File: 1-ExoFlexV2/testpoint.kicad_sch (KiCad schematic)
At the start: 154 parts

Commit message: Schématisation terminée
- Schéma terminé
- Passage vers le PCB
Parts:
- TP1: renamed from TP?; value R1DAMP1 -> TestPoint; DESCRIPTION Compact THM Test Point -Red -> PC TEST POINT COMPACT RED; MANUFACTURER (none) -> Keystone Electronics; PACKAGE NON STANDARD-1 Keystone -> 0.125" Dia x 0.220" L; PART NUMBER (none) -> 5005; TYPE (none) -> Through Hole
- TP10: renamed from TP?; value LLC1 -> TestPoint; DESCRIPTION Compact THM Test Point -Red -> PC TEST POINT COMPACT RED; MANUFACTURER (none) -> Keystone Electronics; PACKAGE NON STANDARD-1 Keystone -> 0.125" Dia x 0.220" L; PART NUMBER (none) -> 5005; TYPE (none) -> Through Hole
- TP100: renamed from TP?; value SSWMAX -> TestPoint; DESCRIPTION Compact THM Test Point -Red -> PC TEST POINT COMPACT RED; MANUFACTURER (none) -> Keystone Electronics; PACKAGE NON STANDARD-1 Keystone -> 0.125" Dia x 0.220" L; PART NUMBER (none) -> 5005; TYPE (none) -> Through Hole
- TP101, TP111, TP112, TP113, TP119, TP120, TP129, TP136, TP137, TP139, TP146, TP148: renamed from TP?; value GND -> TestPoint; DESCRIPTION Compact THM Test Point -Red -> PC TEST POINT COMPACT RED; MANUFACTURER (none) -> Keystone Electronics; PACKAGE NON STANDARD-1 Keystone -> 0.125" Dia x 0.220" L; PART NUMBER (none) -> 5005; TYPE (none) -> Through Hole
- TP102: renamed from TP?; value URG_SEC -> TestPoint; DESCRIPTION Compact THM Test Point -Red -> PC TEST POINT COMPACT RED; MANUFACTURER (none) -> Keystone Electronics; PACKAGE NON STANDARD-1 Keystone -> 0.125" Dia x 0.220" L; PART NUMBER (none) -> 5005; TYPE (none) -> Through Hole
- TP103: renamed from TP?; value SR&L -> TestPoint; DESCRIPTION Compact THM Test Point -Red -> PC TEST POINT COMPACT RED; MANUFACTURER (none) -> Keystone Electronics; PACKAGE NON STANDARD-1 Keystone -> 0.125" Dia x 0.220" L; PART NUMBER (none) -> 5005; TYPE (none) -> Through Hole
- TP104: renamed from TP?; value SINT1 -> TestPoint; DESCRIPTION Compact THM Test Point -Red -> PC TEST POINT COMPACT RED; MANUFACTURER (none) -> Keystone Electronics; PACKAGE NON STANDARD-1 Keystone -> 0.125" Dia x 0.220" L; PART NUMBER (none) -> 5005; TYPE (none) -> Through Hole
- TP105: renamed from TP?; value R1FSR1 -> TestPoint; DESCRIPTION Compact THM Test Point -Red -> PC TEST POINT COMPACT RED; MANUFACTURER (none) -> Keystone Electronics; PACKAGE NON STANDARD-1 Keystone -> 0.125" Dia x 0.220" L; PART NUMBER (none) -> 5005; TYPE (none) -> Through Hole
- TP106: renamed from TP?; value R2FSR1 -> TestPoint; DESCRIPTION Compact THM Test Point -Red -> PC TEST POINT COMPACT RED; MANUFACTURER (none) -> Keystone Electronics; PACKAGE NON STANDARD-1 Keystone -> 0.125" Dia x 0.220" L; PART NUMBER (none) -> 5005; TYPE (none) -> Through Hole
- TP107: renamed from TP?; value R1FSR2 -> TestPoint; DESCRIPTION Compact THM Test Point -Red -> PC TEST POINT COMPACT RED; MANUFACTURER (none) -> Keystone Electronics; PACKAGE NON STANDARD-1 Keystone -> 0.125" Dia x 0.220" L; PART NUMBER (none) -> 5005; TYPE (none) -> Through Hole
- TP108: renamed from TP?; value R2FSR2 -> TestPoint; DESCRIPTION Compact THM Test Point -Red -> PC TEST POINT COMPACT RED; MANUFACTURER (none) -> Keystone Electronics; PACKAGE NON STANDARD-1 Keystone -> 0.125" Dia x 0.220" L; PART NUMBER (none) -> 5005; TYPE (none) -> Through Hole
- TP109: renamed from TP?; value R1FSR3 -> TestPoint; DESCRIPTION Compact THM Test Point -Red -> PC TEST POINT COMPACT RED; MANUFACTURER (none) -> Keystone Electronics; PACKAGE NON STANDARD-1 Keystone -> 0.125" Dia x 0.220" L; PART NUMBER (none) -> 5005; TYPE (none) -> Through Hole
- TP11: renamed from TP?; value CLC1 -> TestPoint; DESCRIPTION Compact THM Test Point -Red -> PC TEST POINT COMPACT RED; MANUFACTURER (none) -> Keystone Electronics; PACKAGE NON STANDARD-1 Keystone -> 0.125" Dia x 0.220" L; PART NUMBER (none) -> 5005; TYPE (none) -> Through Hole
- TP110: renamed from TP?; value R2FSR3 -> TestPoint; DESCRIPTION Compact THM Test Point -Red -> PC TEST POINT COMPACT RED; MANUFACTURER (none) -> Keystone Electronics; PACKAGE NON STANDARD-1 Keystone -> 0.125" Dia x 0.220" L; PART NUMBER (none) -> 5005; TYPE (none) -> Through Hole
- TP114: renamed from TP?; value SINT2 -> TestPoint; DESCRIPTION Compact THM Test Point -Red -> PC TEST POINT COMPACT RED; MANUFACTURER (none) -> Keystone Electronics; PACKAGE NON STANDARD-1 Keystone -> 0.125" Dia x 0.220" L; PART NUMBER (none) -> 5005; TYPE (none) -> Through Hole
- TP115: renamed from TP?; value R1DANA1 -> TestPoint; DESCRIPTION Compact THM Test Point -Red -> PC TEST POINT COMPACT RED; MANUFACTURER (none) -> Keystone Electronics; PACKAGE NON STANDARD-1 Keystone -> 0.125" Dia x 0.220" L; PART NUMBER (none) -> 5005; TYPE (none) -> Through Hole
- TP116: renamed from TP?; value R2DANA1 -> TestPoint; DESCRIPTION Compact THM Test Point -Red -> PC TEST POINT COMPACT RED; MANUFACTURER (none) -> Keystone Electronics; PACKAGE NON STANDARD-1 Keystone -> 0.125" Dia x 0.220" L; PART NUMBER (none) -> 5005; TYPE (none) -> Through Hole
- TP117: renamed from TP?; value R1DANA2 -> TestPoint; DESCRIPTION Compact THM Test Point -Red -> PC TEST POINT COMPACT RED; MANUFACTURER (none) -> Keystone Electronics; PACKAGE NON STANDARD-1 Keystone -> 0.125" Dia x 0.220" L; PART NUMBER (none) -> 5005; TYPE (none) -> Through Hole
- TP118: renamed from TP?; value R2DANA2 -> TestPoint; DESCRIPTION Compact THM Test Point -Red -> PC TEST POINT COMPACT RED; MANUFACTURER (none) -> Keystone Electronics; PACKAGE NON STANDARD-1 Keystone -> 0.125" Dia x 0.220" L; PART NUMBER (none) -> 5005; TYPE (none) -> Through Hole
- TP12: renamed from TP?; value R1DAMP2 -> TestPoint; DESCRIPTION Compact THM Test Point -Red -> PC TEST POINT COMPACT RED; MANUFACTURER (none) -> Keystone Electronics; PACKAGE NON STANDARD-1 Keystone -> 0.125" Dia x 0.220" L; PART NUMBER (none) -> 5005; TYPE (none) -> Through Hole
- TP121: renamed from TP?; value SINT3 -> TestPoint; DESCRIPTION Compact THM Test Point -Red -> PC TEST POINT COMPACT RED; MANUFACTURER (none) -> Keystone Electronics; PACKAGE NON STANDARD-1 Keystone -> 0.125" Dia x 0.220" L; PART NUMBER (none) -> 5005; TYPE (none) -> Through Hole
- TP122: renamed from TP?; value 24V -> TestPoint; DESCRIPTION Compact THM Test Point -Red -> PC TEST POINT COMPACT RED; MANUFACTURER (none) -> Keystone Electronics; PACKAGE NON STANDARD-1 Keystone -> 0.125" Dia x 0.220" L; PART NUMBER (none) -> 5005; TYPE (none) -> Through Hole
- TP123: renamed from TP?; value 5VNUM -> TestPoint; DESCRIPTION Compact THM Test Point -Red -> PC TEST POINT COMPACT RED; MANUFACTURER (none) -> Keystone Electronics; PACKAGE NON STANDARD-1 Keystone -> 0.125" Dia x 0.220" L; PART NUMBER (none) -> 5005; TYPE (none) -> Through Hole
- TP124: renamed from TP?; value R1EM2 -> TestPoint; DESCRIPTION Compact THM Test Point -Red -> PC TEST POINT COMPACT RED; MANUFACTURER (none) -> Keystone Electronics; PACKAGE NON STANDARD-1 Keystone -> 0.125" Dia x 0.220" L; PART NUMBER (none) -> 5005; TYPE (none) -> Through Hole
- TP125: renamed from TP?; value R2EM2 -> TestPoint; DESCRIPTION Compact THM Test Point -Red -> PC TEST POINT COMPACT RED; MANUFACTURER (none) -> Keystone Electronics; PACKAGE NON STANDARD-1 Keystone -> 0.125" Dia x 0.220" L; PART NUMBER (none) -> 5005; TYPE (none) -> Through Hole
- TP126: renamed from TP?; value BUTPROXL1 -> TestPoint; DESCRIPTION Compact THM Test Point -Red -> PC TEST POINT COMPACT RED; MANUFACTURER (none) -> Keystone Electronics; PACKAGE NON STANDARD-1 Keystone -> 0.125" Dia x 0.220" L; PART NUMBER (none) -> 5005; TYPE (none) -> Through Hole
- TP127: renamed from TP?; value BUTPROXR2 -> TestPoint; DESCRIPTION Compact THM Test Point -Red -> PC TEST POINT COMPACT RED; MANUFACTURER (none) -> Keystone Electronics; PACKAGE NON STANDARD-1 Keystone -> 0.125" Dia x 0.220" L; PART NUMBER (none) -> 5005; TYPE (none) -> Through Hole
- TP128: renamed from TP?; value DSW&INT -> TestPoint; DESCRIPTION Compact THM Test Point -Red -> PC TEST POINT COMPACT RED; MANUFACTURER (none) -> Keystone Electronics; PACKAGE NON STANDARD-1 Keystone -> 0.125" Dia x 0.220" L; PART NUMBER (none) -> 5005; TYPE (none) -> Through Hole
- TP13: renamed from TP?; value R2DAMP2 -> TestPoint; DESCRIPTION Compact THM Test Point -Red -> PC TEST POINT COMPACT RED; MANUFACTURER (none) -> Keystone Electronics; PACKAGE NON STANDARD-1 Keystone -> 0.125" Dia x 0.220" L; PART NUMBER (none) -> 5005; TYPE (none) -> Through Hole
- TP130: renamed from TP?; value RELAY -> TestPoint; DESCRIPTION Compact THM Test Point -Red -> PC TEST POINT COMPACT RED; MANUFACTURER (none) -> Keystone Electronics; PACKAGE NON STANDARD-1 Keystone -> 0.125" Dia x 0.220" L; PART NUMBER (none) -> 5005; TYPE (none) -> Through Hole
- TP131: renamed from TP?; value RESET -> TestPoint; DESCRIPTION Compact THM Test Point -Red -> PC TEST POINT COMPACT RED; MANUFACTURER (none) -> Keystone Electronics; PACKAGE NON STANDARD-1 Keystone -> 0.125" Dia x 0.220" L; PART NUMBER (none) -> 5005; TYPE (none) -> Through Hole
- TP132: renamed from TP?; value R1RE2 -> TestPoint; DESCRIPTION Compact THM Test Point -Red -> PC TEST POINT COMPACT RED; MANUFACTURER (none) -> Keystone Electronics; PACKAGE NON STANDARD-1 Keystone -> 0.125" Dia x 0.220" L; PART NUMBER (none) -> 5005; TYPE (none) -> Through Hole
- TP133: renamed from TP?; value R2RE2 -> TestPoint; DESCRIPTION Compact THM Test Point -Red -> PC TEST POINT COMPACT RED; MANUFACTURER (none) -> Keystone Electronics; PACKAGE NON STANDARD-1 Keystone -> 0.125" Dia x 0.220" L; PART NUMBER (none) -> 5005; TYPE (none) -> Through Hole
- TP134: renamed from TP?; value BUTPROXL2 -> TestPoint; DESCRIPTION Compact THM Test Point -Red -> PC TEST POINT COMPACT RED; MANUFACTURER (none) -> Keystone Electronics; PACKAGE NON STANDARD-1 Keystone -> 0.125" Dia x 0.220" L; PART NUMBER (none) -> 5005; TYPE (none) -> Through Hole
- TP135: renamed from TP?; value OPTO1 -> TestPoint; DESCRIPTION Compact THM Test Point -Red -> PC TEST POINT COMPACT RED; MANUFACTURER (none) -> Keystone Electronics; PACKAGE NON STANDARD-1 Keystone -> 0.125" Dia x 0.220" L; PART NUMBER (none) -> 5005; TYPE (none) -> Through Hole
- TP138: renamed from TP?; value CAN_RD -> TestPoint; DESCRIPTION Compact THM Test Point -Red -> PC TEST POINT COMPACT RED; MANUFACTURER (none) -> Keystone Electronics; PACKAGE NON STANDARD-1 Keystone -> 0.125" Dia x 0.220" L; PART NUMBER (none) -> 5005; TYPE (none) -> Through Hole
- TP14: renamed from TP?; value R1DLAMP2 -> TestPoint; DESCRIPTION Compact THM Test Point -Red -> PC TEST POINT COMPACT RED; MANUFACTURER (none) -> Keystone Electronics; PACKAGE NON STANDARD-1 Keystone -> 0.125" Dia x 0.220" L; PART NUMBER (none) -> 5005; TYPE (none) -> Through Hole
- TP140: renamed from TP?; value 5VA -> TestPoint; DESCRIPTION Compact THM Test Point -Red -> PC TEST POINT COMPACT RED; MANUFACTURER (none) -> Keystone Electronics; PACKAGE NON STANDARD-1 Keystone -> 0.125" Dia x 0.220" L; PART NUMBER (none) -> 5005; TYPE (none) -> Through Hole
- TP141: renamed from TP?; value 5VA- -> TestPoint; DESCRIPTION Compact THM Test Point -Red -> PC TEST POINT COMPACT RED; MANUFACTURER (none) -> Keystone Electronics; PACKAGE NON STANDARD-1 Keystone -> 0.125" Dia x 0.220" L; PART NUMBER (none) -> 5005; TYPE (none) -> Through Hole
- TP142: renamed from TP?; value R1EM1 -> TestPoint; DESCRIPTION Compact THM Test Point -Red -> PC TEST POINT COMPACT RED; MANUFACTURER (none) -> Keystone Electronics; PACKAGE NON STANDARD-1 Keystone -> 0.125" Dia x 0.220" L; PART NUMBER (none) -> 5005; TYPE (none) -> Through Hole
- TP143: renamed from TP?; value R2EM1 -> TestPoint; DESCRIPTION Compact THM Test Point -Red -> PC TEST POINT COMPACT RED; MANUFACTURER (none) -> Keystone Electronics; PACKAGE NON STANDARD-1 Keystone -> 0.125" Dia x 0.220" L; PART NUMBER (none) -> 5005; TYPE (none) -> Through Hole
- TP144: renamed from TP?; value BUTPROXR1 -> TestPoint; DESCRIPTION Compact THM Test Point -Red -> PC TEST POINT COMPACT RED; MANUFACTURER (none) -> Keystone Electronics; PACKAGE NON STANDARD-1 Keystone -> 0.125" Dia x 0.220" L; PART NUMBER (none) -> 5005; TYPE (none) -> Through Hole
- TP145: renamed from TP?; value OPTO2 -> TestPoint; DESCRIPTION Compact THM Test Point -Red -> PC TEST POINT COMPACT RED; MANUFACTURER (none) -> Keystone Electronics; PACKAGE NON STANDARD-1 Keystone -> 0.125" Dia x 0.220" L; PART NUMBER (none) -> 5005; TYPE (none) -> Through Hole
- TP147: renamed from TP?; value CAN_TD -> TestPoint; DESCRIPTION Compact THM Test Point -Red -> PC TEST POINT COMPACT RED; MANUFACTURER (none) -> Keystone Electronics; PACKAGE NON STANDARD-1 Keystone -> 0.125" Dia x 0.220" L; PART NUMBER (none) -> 5005; TYPE (none) -> Through Hole
- TP149: renamed from TP?; value LATCH -> TestPoint; DESCRIPTION Compact THM Test Point -Red -> PC TEST POINT COMPACT RED; MANUFACTURER (none) -> Keystone Electronics; PACKAGE NON STANDARD-1 Keystone -> 0.125" Dia x 0.220" L; PART NUMBER (none) -> 5005; TYPE (none) -> Through Hole
- TP15: renamed from TP?; value R2DLAMP2 -> TestPoint; DESCRIPTION Compact THM Test Point -Red -> PC TEST POINT COMPACT RED; MANUFACTURER (none) -> Keystone Electronics; PACKAGE NON STANDARD-1 Keystone -> 0.125" Dia x 0.220" L; PART NUMBER (none) -> 5005; TYPE (none) -> Through Hole
- TP150, TP33: renamed from TP?; value SALIM -> TestPoint; DESCRIPTION Compact THM Test Point -Red -> PC TEST POINT COMPACT RED; MANUFACTURER (none) -> Keystone Electronics; PACKAGE NON STANDARD-1 Keystone -> 0.125" Dia x 0.220" L; PART NUMBER (none) -> 5005; TYPE (none) -> Through Hole
- TP151: renamed from TP?; value R1RE1 -> TestPoint; DESCRIPTION Compact THM Test Point -Red -> PC TEST POINT COMPACT RED; MANUFACTURER (none) -> Keystone Electronics; PACKAGE NON STANDARD-1 Keystone -> 0.125" Dia x 0.220" L; PART NUMBER (none) -> 5005; TYPE (none) -> Through Hole
- TP152: renamed from TP?; value R2RE1 -> TestPoint; DESCRIPTION Compact THM Test Point -Red -> PC TEST POINT COMPACT RED; MANUFACTURER (none) -> Keystone Electronics; PACKAGE NON STANDARD-1 Keystone -> 0.125" Dia x 0.220" L; PART NUMBER (none) -> 5005; TYPE (none) -> Through Hole
- TP153: renamed from TP?; value SOPTO -> TestPoint; DESCRIPTION Compact THM Test Point -Red -> PC TEST POINT COMPACT RED; MANUFACTURER (none) -> Keystone Electronics; PACKAGE NON STANDARD-1 Keystone -> 0.125" Dia x 0.220" L; PART NUMBER (none) -> 5005; TYPE (none) -> Through Hole
- TP154: renamed from TP?; value SBUTPROX -> TestPoint; DESCRIPTION Compact THM Test Point -Red -> PC TEST POINT COMPACT RED; MANUFACTURER (none) -> Keystone Electronics; PACKAGE NON STANDARD-1 Keystone -> 0.125" Dia x 0.220" L; PART NUMBER (none) -> 5005; TYPE (none) -> Through Hole
- TP16: renamed from TP?; value SGAMP2 -> TestPoint; DESCRIPTION Compact THM Test Point -Red -> PC TEST POINT COMPACT RED; MANUFACTURER (none) -> Keystone Electronics; PACKAGE NON STANDARD-1 Keystone -> 0.125" Dia x 0.220" L; PART NUMBER (none) -> 5005; TYPE (none) -> Through Hole
- TP17: renamed from TP?; value LAMP2 -> TestPoint; DESCRIPTION Compact THM Test Point -Red -> PC TEST POINT COMPACT RED; MANUFACTURER (none) -> Keystone Electronics; PACKAGE NON STANDARD-1 Keystone -> 0.125" Dia x 0.220" L; PART NUMBER (none) -> 5005; TYPE (none) -> Through Hole
- TP18: renamed from TP?; value CAMP2 -> TestPoint; DESCRIPTION Compact THM Test Point -Red -> PC TEST POINT COMPACT RED; MANUFACTURER (none) -> Keystone Electronics; PACKAGE NON STANDARD-1 Keystone -> 0.125" Dia x 0.220" L; PART NUMBER (none) -> 5005; TYPE (none) -> Through Hole
- TP19: renamed from TP?; value SGLC2 -> TestPoint; DESCRIPTION Compact THM Test Point -Red -> PC TEST POINT COMPACT RED; MANUFACTURER (none) -> Keystone Electronics; PACKAGE NON STANDARD-1 Keystone -> 0.125" Dia x 0.220" L; PART NUMBER (none) -> 5005; TYPE (none) -> Through Hole
- TP2: renamed from TP?; value R2DAMP1 -> TestPoint; DESCRIPTION Compact THM Test Point -Red -> PC TEST POINT COMPACT RED; MANUFACTURER (none) -> Keystone Electronics; PACKAGE NON STANDARD-1 Keystone -> 0.125" Dia x 0.220" L; PART NUMBER (none) -> 5005; TYPE (none) -> Through Hole
- TP20: renamed from TP?; value LLC2 -> TestPoint; DESCRIPTION Compact THM Test Point -Red -> PC TEST POINT COMPACT RED; MANUFACTURER (none) -> Keystone Electronics; PACKAGE NON STANDARD-1 Keystone -> 0.125" Dia x 0.220" L; PART NUMBER (none) -> 5005; TYPE (none) -> Through Hole
- TP21: renamed from TP?; value CLC2 -> TestPoint; DESCRIPTION Compact THM Test Point -Red -> PC TEST POINT COMPACT RED; MANUFACTURER (none) -> Keystone Electronics; PACKAGE NON STANDARD-1 Keystone -> 0.125" Dia x 0.220" L; PART NUMBER (none) -> 5005; TYPE (none) -> Through Hole
- TP22: renamed from TP?; value SGLC3 -> TestPoint; DESCRIPTION Compact THM Test Point -Red -> PC TEST POINT COMPACT RED; MANUFACTURER (none) -> Keystone Electronics; PACKAGE NON STANDARD-1 Keystone -> 0.125" Dia x 0.220" L; PART NUMBER (none) -> 5005; TYPE (none) -> Through Hole
- TP23: renamed from TP?; value LLC3 -> TestPoint; DESCRIPTION Compact THM Test Point -Red -> PC TEST POINT COMPACT RED; MANUFACTURER (none) -> Keystone Electronics; PACKAGE NON STANDARD-1 Keystone -> 0.125" Dia x 0.220" L; PART NUMBER (none) -> 5005; TYPE (none) -> Through Hole
- TP24: renamed from TP?; value CLC3 -> TestPoint; DESCRIPTION Compact THM Test Point -Red -> PC TEST POINT COMPACT RED; MANUFACTURER (none) -> Keystone Electronics; PACKAGE NON STANDARD-1 Keystone -> 0.125" Dia x 0.220" L; PART NUMBER (none) -> 5005; TYPE (none) -> Through Hole
- TP25: renamed from TP?; value SLCPOS -> TestPoint; DESCRIPTION Compact THM Test Point -Red -> PC TEST POINT COMPACT RED; MANUFACTURER (none) -> Keystone Electronics; PACKAGE NON STANDARD-1 Keystone -> 0.125" Dia x 0.220" L; PART NUMBER (none) -> 5005; TYPE (none) -> Through Hole
- TP26: renamed from TP?; value R1DAMP3 -> TestPoint; DESCRIPTION Compact THM Test Point -Red -> PC TEST POINT COMPACT RED; MANUFACTURER (none) -> Keystone Electronics; PACKAGE NON STANDARD-1 Keystone -> 0.125" Dia x 0.220" L; PART NUMBER (none) -> 5005; TYPE (none) -> Through Hole
- TP27: renamed from TP?; value R2DAMP3 -> TestPoint; DESCRIPTION Compact THM Test Point -Red -> PC TEST POINT COMPACT RED; MANUFACTURER (none) -> Keystone Electronics; PACKAGE NON STANDARD-1 Keystone -> 0.125" Dia x 0.220" L; PART NUMBER (none) -> 5005; TYPE (none) -> Through Hole
- TP28: renamed from TP?; value R1DLAMP3 -> TestPoint; DESCRIPTION Compact THM Test Point -Red -> PC TEST POINT COMPACT RED; MANUFACTURER (none) -> Keystone Electronics; PACKAGE NON STANDARD-1 Keystone -> 0.125" Dia x 0.220" L; PART NUMBER (none) -> 5005; TYPE (none) -> Through Hole
- TP29: renamed from TP?; value R2DLAMP3 -> TestPoint; DESCRIPTION Compact THM Test Point -Red -> PC TEST POINT COMPACT RED; MANUFACTURER (none) -> Keystone Electronics; PACKAGE NON STANDARD-1 Keystone -> 0.125" Dia x 0.220" L; PART NUMBER (none) -> 5005; TYPE (none) -> Through Hole
- TP3: renamed from TP?; value R1DLAMP1 -> TestPoint; DESCRIPTION Compact THM Test Point -Red -> PC TEST POINT COMPACT RED; MANUFACTURER (none) -> Keystone Electronics; PACKAGE NON STANDARD-1 Keystone -> 0.125" Dia x 0.220" L; PART NUMBER (none) -> 5005; TYPE (none) -> Through Hole
- TP30: renamed from TP?; value SGAMP3 -> TestPoint; DESCRIPTION Compact THM Test Point -Red -> PC TEST POINT COMPACT RED; MANUFACTURER (none) -> Keystone Electronics; PACKAGE NON STANDARD-1 Keystone -> 0.125" Dia x 0.220" L; PART NUMBER (none) -> 5005; TYPE (none) -> Through Hole
- TP31: renamed from TP?; value LAMP3 -> TestPoint; DESCRIPTION Compact THM Test Point -Red -> PC TEST POINT COMPACT RED; MANUFACTURER (none) -> Keystone Electronics; PACKAGE NON STANDARD-1 Keystone -> 0.125" Dia x 0.220" L; PART NUMBER (none) -> 5005; TYPE (none) -> Through Hole
- TP32: renamed from TP?; value CAMP3 -> TestPoint; DESCRIPTION Compact THM Test Point -Red -> PC TEST POINT COMPACT RED; MANUFACTURER (none) -> Keystone Electronics; PACKAGE NON STANDARD-1 Keystone -> 0.125" Dia x 0.220" L; PART NUMBER (none) -> 5005; TYPE (none) -> Through Hole
- TP34: renamed from TP?; value SGTEMP1 -> TestPoint; DESCRIPTION Compact THM Test Point -Red -> PC TEST POINT COMPACT RED; MANUFACTURER (none) -> Keystone Electronics; PACKAGE NON STANDARD-1 Keystone -> 0.125" Dia x 0.220" L; PART NUMBER (none) -> 5005; TYPE (none) -> Through Hole
- TP35: renamed from TP?; value LTEMP1 -> TestPoint; DESCRIPTION Compact THM Test Point -Red -> PC TEST POINT COMPACT RED; MANUFACTURER (none) -> Keystone Electronics; PACKAGE NON STANDARD-1 Keystone -> 0.125" Dia x 0.220" L; PART NUMBER (none) -> 5005; TYPE (none) -> Through Hole
- TP36: renamed from TP?; value R1IST1 -> TestPoint; DESCRIPTION Compact THM Test Point -Red -> PC TEST POINT COMPACT RED; MANUFACTURER (none) -> Keystone Electronics; PACKAGE NON STANDARD-1 Keystone -> 0.125" Dia x 0.220" L; PART NUMBER (none) -> 5005; TYPE (none) -> Through Hole
- TP37: renamed from TP?; value R2IST1 -> TestPoint; DESCRIPTION Compact THM Test Point -Red -> PC TEST POINT COMPACT RED; MANUFACTURER (none) -> Keystone Electronics; PACKAGE NON STANDARD-1 Keystone -> 0.125" Dia x 0.220" L; PART NUMBER (none) -> 5005; TYPE (none) -> Through Hole
- TP38: renamed from TP?; value R1DLTOR1 -> TestPoint; DESCRIPTION Compact THM Test Point -Red -> PC TEST POINT COMPACT RED; MANUFACTURER (none) -> Keystone Electronics; PACKAGE NON STANDARD-1 Keystone -> 0.125" Dia x 0.220" L; PART NUMBER (none) -> 5005; TYPE (none) -> Through Hole
- TP39: renamed from TP?; value R2DLTOR1 -> TestPoint; DESCRIPTION Compact THM Test Point -Red -> PC TEST POINT COMPACT RED; MANUFACTURER (none) -> Keystone Electronics; PACKAGE NON STANDARD-1 Keystone -> 0.125" Dia x 0.220" L; PART NUMBER (none) -> 5005; TYPE (none) -> Through Hole
- TP4: renamed from TP?; value R2DLAMP1 -> TestPoint; DESCRIPTION Compact THM Test Point -Red -> PC TEST POINT COMPACT RED; MANUFACTURER (none) -> Keystone Electronics; PACKAGE NON STANDARD-1 Keystone -> 0.125" Dia x 0.220" L; PART NUMBER (none) -> 5005; TYPE (none) -> Through Hole
- TP40: renamed from TP?; value SGTOR1 -> TestPoint; DESCRIPTION Compact THM Test Point -Red -> PC TEST POINT COMPACT RED; MANUFACTURER (none) -> Keystone Electronics; PACKAGE NON STANDARD-1 Keystone -> 0.125" Dia x 0.220" L; PART NUMBER (none) -> 5005; TYPE (none) -> Through Hole
- TP41: renamed from TP?; value LTOR1 -> TestPoint; DESCRIPTION Compact THM Test Point -Red -> PC TEST POINT COMPACT RED; MANUFACTURER (none) -> Keystone Electronics; PACKAGE NON STANDARD-1 Keystone -> 0.125" Dia x 0.220" L; PART NUMBER (none) -> 5005; TYPE (none) -> Through Hole
- TP42, TP7: renamed from TP?; value CAMP1 -> TestPoint; DESCRIPTION Compact THM Test Point -Red -> PC TEST POINT COMPACT RED; MANUFACTURER (none) -> Keystone Electronics; PACKAGE NON STANDARD-1 Keystone -> 0.125" Dia x 0.220" L; PART NUMBER (none) -> 5005; TYPE (none) -> Through Hole
- TP43: renamed from TP?; value STOR -> TestPoint; DESCRIPTION Compact THM Test Point -Red -> PC TEST POINT COMPACT RED; MANUFACTURER (none) -> Keystone Electronics; PACKAGE NON STANDARD-1 Keystone -> 0.125" Dia x 0.220" L; PART NUMBER (none) -> 5005; TYPE (none) -> Through Hole
- TP44: renamed from TP?; value SGFSR1 -> TestPoint; DESCRIPTION Compact THM Test Point -Red -> PC TEST POINT COMPACT RED; MANUFACTURER (none) -> Keystone Electronics; PACKAGE NON STANDARD-1 Keystone -> 0.125" Dia x 0.220" L; PART NUMBER (none) -> 5005; TYPE (none) -> Through Hole
- TP45: renamed from TP?; value LFSR1 -> TestPoint; DESCRIPTION Compact THM Test Point -Red -> PC TEST POINT COMPACT RED; MANUFACTURER (none) -> Keystone Electronics; PACKAGE NON STANDARD-1 Keystone -> 0.125" Dia x 0.220" L; PART NUMBER (none) -> 5005; TYPE (none) -> Through Hole
- TP46: renamed from TP?; value CFSR1 -> TestPoint; DESCRIPTION Compact THM Test Point -Red -> PC TEST POINT COMPACT RED; MANUFACTURER (none) -> Keystone Electronics; PACKAGE NON STANDARD-1 Keystone -> 0.125" Dia x 0.220" L; PART NUMBER (none) -> 5005; TYPE (none) -> Through Hole
- TP47: renamed from TP?; value CTEMP1 -> TestPoint; DESCRIPTION Compact THM Test Point -Red -> PC TEST POINT COMPACT RED; MANUFACTURER (none) -> Keystone Electronics; PACKAGE NON STANDARD-1 Keystone -> 0.125" Dia x 0.220" L; PART NUMBER (none) -> 5005; TYPE (none) -> Through Hole
- TP48: renamed from TP?; value R1IST2 -> TestPoint; DESCRIPTION Compact THM Test Point -Red -> PC TEST POINT COMPACT RED; MANUFACTURER (none) -> Keystone Electronics; PACKAGE NON STANDARD-1 Keystone -> 0.125" Dia x 0.220" L; PART NUMBER (none) -> 5005; TYPE (none) -> Through Hole
- TP49: renamed from TP?; value R2IST2 -> TestPoint; DESCRIPTION Compact THM Test Point -Red -> PC TEST POINT COMPACT RED; MANUFACTURER (none) -> Keystone Electronics; PACKAGE NON STANDARD-1 Keystone -> 0.125" Dia x 0.220" L; PART NUMBER (none) -> 5005; TYPE (none) -> Through Hole
- TP5: renamed from TP?; value SGAMP1 -> TestPoint; DESCRIPTION Compact THM Test Point -Red -> PC TEST POINT COMPACT RED; MANUFACTURER (none) -> Keystone Electronics; PACKAGE NON STANDARD-1 Keystone -> 0.125" Dia x 0.220" L; PART NUMBER (none) -> 5005; TYPE (none) -> Through Hole
- TP50: renamed from TP?; value R1DLTOR2 -> TestPoint; DESCRIPTION Compact THM Test Point -Red -> PC TEST POINT COMPACT RED; MANUFACTURER (none) -> Keystone Electronics; PACKAGE NON STANDARD-1 Keystone -> 0.125" Dia x 0.220" L; PART NUMBER (none) -> 5005; TYPE (none) -> Through Hole
- TP51: renamed from TP?; value R2DLTOR2 -> TestPoint; DESCRIPTION Compact THM Test Point -Red -> PC TEST POINT COMPACT RED; MANUFACTURER (none) -> Keystone Electronics; PACKAGE NON STANDARD-1 Keystone -> 0.125" Dia x 0.220" L; PART NUMBER (none) -> 5005; TYPE (none) -> Through Hole
- TP52: renamed from TP?; value SGTOR2 -> TestPoint; DESCRIPTION Compact THM Test Point -Red -> PC TEST POINT COMPACT RED; MANUFACTURER (none) -> Keystone Electronics; PACKAGE NON STANDARD-1 Keystone -> 0.125" Dia x 0.220" L; PART NUMBER (none) -> 5005; TYPE (none) -> Through Hole
- TP53: renamed from TP?; value LTOR2 -> TestPoint; DESCRIPTION Compact THM Test Point -Red -> PC TEST POINT COMPACT RED; MANUFACTURER (none) -> Keystone Electronics; PACKAGE NON STANDARD-1 Keystone -> 0.125" Dia x 0.220" L; PART NUMBER (none) -> 5005; TYPE (none) -> Through Hole
- TP54: renamed from TP?; value CTOR2 -> TestPoint; DESCRIPTION Compact THM Test Point -Red -> PC TEST POINT COMPACT RED; MANUFACTURER (none) -> Keystone Electronics; PACKAGE NON STANDARD-1 Keystone -> 0.125" Dia x 0.220" L; PART NUMBER (none) -> 5005; TYPE (none) -> Through Hole
- TP55: renamed from TP?; value SGFSR2 -> TestPoint; DESCRIPTION Compact THM Test Point -Red -> PC TEST POINT COMPACT RED; MANUFACTURER (none) -> Keystone Electronics; PACKAGE NON STANDARD-1 Keystone -> 0.125" Dia x 0.220" L; PART NUMBER (none) -> 5005; TYPE (none) -> Through Hole
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
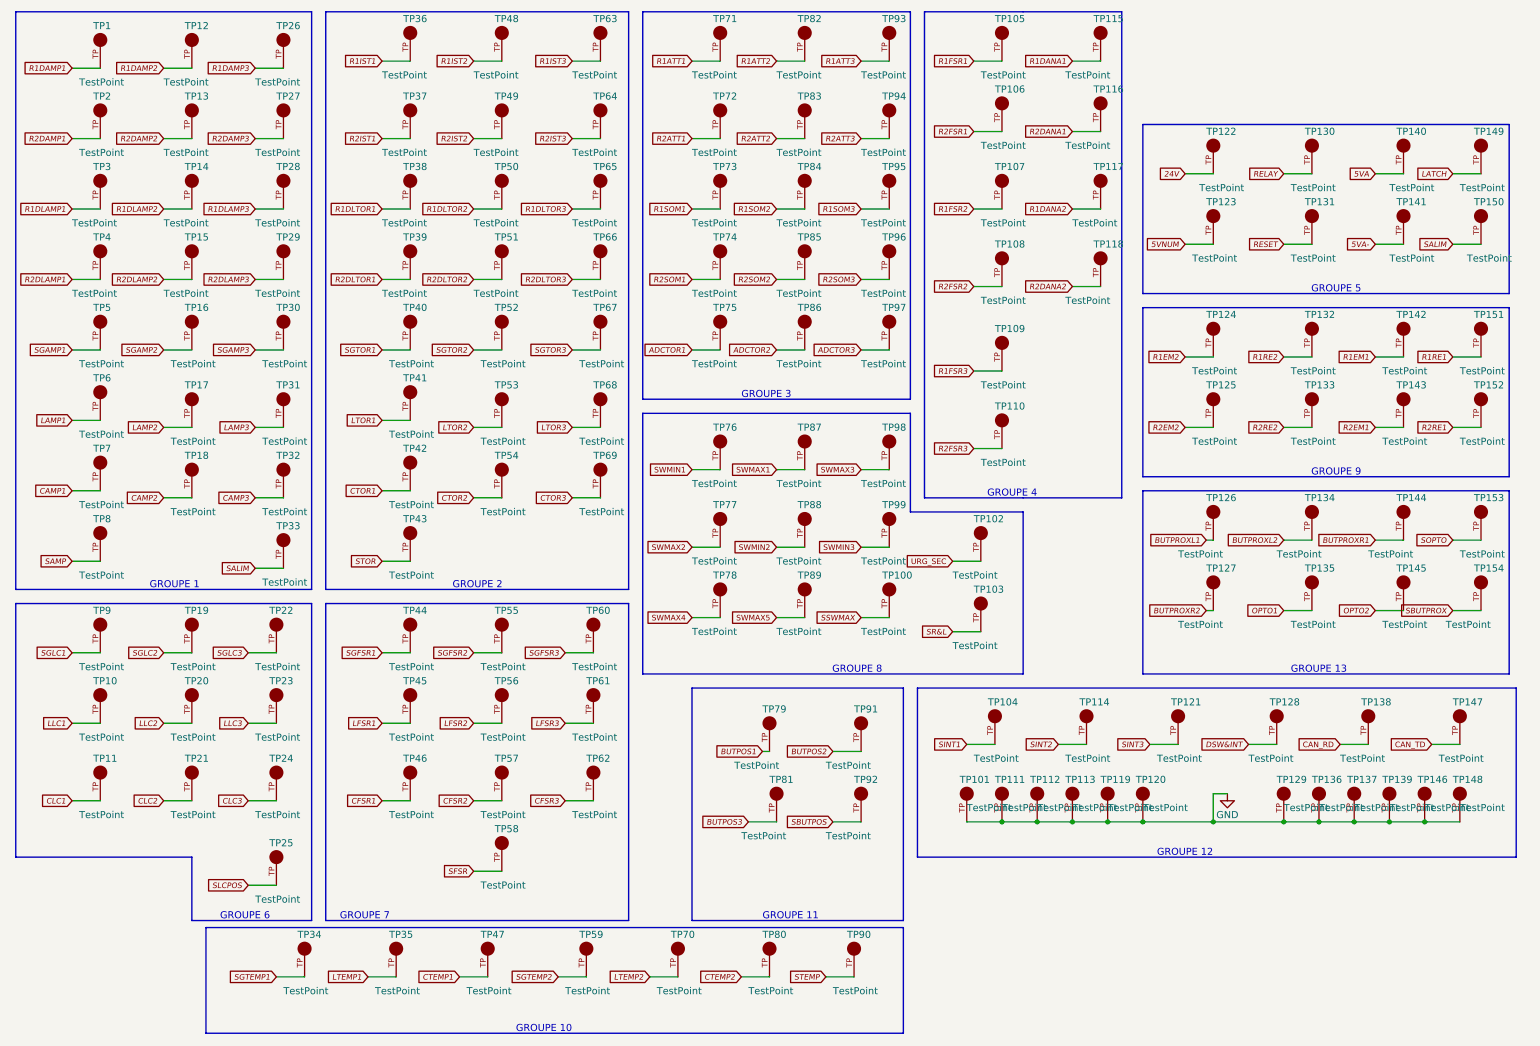
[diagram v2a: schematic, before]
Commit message: Finalisation 3
- Changement des régulateur de tension
- Retrait de test point inutile
- Changement de jumper mal positionner
- Ajout de Mounting holes et fiducial
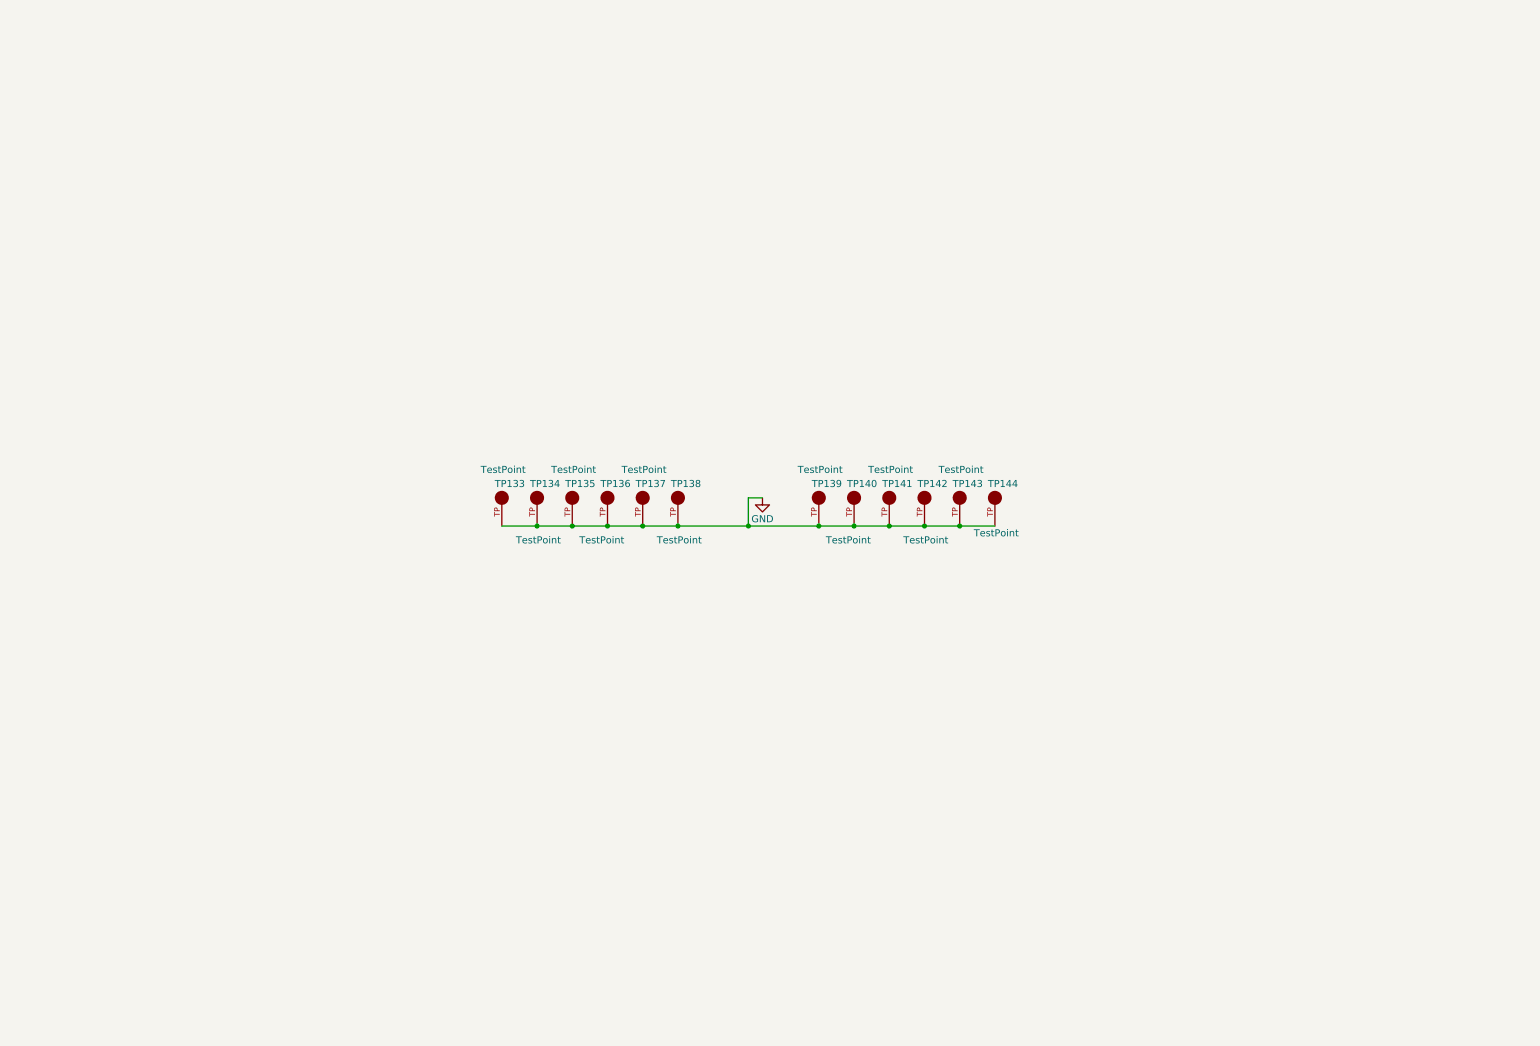
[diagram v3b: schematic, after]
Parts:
- removed TP1, TP10, TP100, TP101, TP102, TP103, TP104, TP105, TP106, TP107, TP108, TP109, TP11, TP110, TP111, TP112, TP113, TP114, TP115, TP116, TP117, TP118, TP119, TP12, TP120, TP121, TP122, TP123, TP124, TP125, TP126, TP127, TP128, TP129, TP13, TP130, TP131, TP132, TP14, TP145, TP146, TP147, TP148, TP149, TP15, TP150, TP151, TP152, TP153, TP154, TP16, TP17, TP18, TP19, TP2, TP20, TP21, TP22, TP23, TP24, TP25, TP26, TP27, TP28, TP29, TP3, TP30, TP31, TP32, TP33, TP34, TP35, TP36, TP37, TP38, TP39, TP4, TP40, TP41, TP42, TP43, TP44, TP45, TP46, TP47, TP48, TP49, TP5, TP50, TP51, TP52, TP53, TP54, TP55, TP56, TP57, TP58, TP59, TP6, TP60, TP61, TP62, TP63, TP64, TP65, TP66, TP67, TP68, TP69, TP7, TP70, TP71, TP72, TP73, TP74, TP75, TP76, TP77, TP78, TP79, TP8, TP80, TP81, TP82, TP83, TP84, TP85, TP86, TP87, TP88, TP89, TP9, TP90, TP91, TP92, TP93, TP94, TP95, TP96, TP97, TP98, TP99: TestPoint, FootPrint:KEYSTONE_5005, symbol SymLib:5005
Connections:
- net 5VA is gone; now on net GND: TP140.TP
- net 5VA- is gone; now on net GND: TP141.TP
- net BUTPROXL2 is gone; now on net GND: TP134.TP
- net BUTPROXR1 is gone; now on net GND: TP144.TP
- net CAN_RD is gone; now on net GND: TP138.TP
- net OPTO1 is gone; now on net GND: TP135.TP
- net R1EM1 is gone; now on net GND: TP142.TP
- net R2EM1 is gone; now on net GND: TP143.TP
- net R2RE2 is gone; now on net GND: TP133.TP
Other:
- note removed: "GROUPE 1"
- note removed: "GROUPE 10"
- note removed: "GROUPE 11"
- note removed: "GROUPE 12"
- note removed: "GROUPE 13"
- note removed: "GROUPE 2"
- note removed: "GROUPE 3"
- note removed: "GROUPE 4"
- note removed: "GROUPE 5"
- note removed: "GROUPE 6"
- note removed: "GROUPE 7"
- note removed: "GROUPE 8"
- note removed: "GROUPE 9"

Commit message: Finalisation schéma FIN
- Changement des uméro pour les inverseurs
- Changement des connecteur et début de placement
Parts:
- TP133, TP134, TP135, TP136, TP137, TP138, TP139, TP140, TP141, TP142, TP143, TP144: NOTES (none) -> DO NOT POPULATE; PURCHASE-URL https://pricing.snapeda.com/search/part/5005/?ref=eda -> (none)
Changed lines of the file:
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@@
       (effects (font (size 1.27 1.27)) (justify bottom) hide)
     )
-    (property "PURCHASE-URL" "https://pricing.snapeda.com/search/part/5005/?ref=eda" (id 10) (at 158.75 100.33 0)
+    (property "PURCHASE-URL" "" (id 10) (at 158.75 100.33 0)
       (effects (font (size 1.27 1.27)) (justify bottom) hide)
     )
@@
     )
     (property "TYPE" "Through Hole" (id 13) (at 158.75 100.33 0)
+      (effects (font (size 1.27 1.27)) hide)
+    )
+    (property "NOTES" "DO NOT POPULATE" (id 14) (at 158.75 100.33 0)
       (effects (font (size 1.27 1.27)) hide)
     )
@@
       (effects (font (size 1.27 1.27)) (justify bottom) hide)
     )
-    (property "PURCHASE-URL" "https://pricing.snapeda.com/search/part/5005/?ref=eda" (id 10) (at 171.45 100.33 0)
+    (property "PURCHASE-URL" "" (id 10) (at 171.45 100.33 0)
       (effects (font (size 1.27 1.27)) (justify bottom) hide)
     )
@@
       (effects (font (size 1.27 1.27)) hide)
     )
+    (property "NOTES" "DO NOT POPULATE" (id 14) (at 171.45 100.33 0)
+      (effects (font (size 1.27 1.27)) hide)
+    )
     (pin "TP")
   )
@@
       (effects (font (size 1.27 1.27)) (justify bottom) hide)
     )
-    (property "PURCHASE-URL" "https://pricing.snapeda.com/search/part/5005/?ref=eda" (id 10) (at 133.35 100.33 0)
+    (property "PURCHASE-URL" "" (id 10) (at 133.35 100.33 0)
       (effects (font (size 1.27 1.27)) (justify bottom) hide)
     )
@@
       (effects (font (size 1.27 1.27)) hide)
     )
+    (property "NOTES" "DO NOT POPULATE" (id 14) (at 133.35 100.33 0)
+      (effects (font (size 1.27 1.27)) hide)
+    )
     (pin "TP")
   )
@@
       (effects (font (size 1.27 1.27)) (justify bottom) hide)
     )
-    (property "PURCHASE-URL" "https://pricing.snapeda.com/search/part/5005/?ref=eda" (id 10) (at 101.6 100.33 0)
+    (property "PURCHASE-URL" "" (id 10) (at 101.6 100.33 0)
       (effects (font (size 1.27 1.27)) (justify bottom) hide)
     )
@@
       (effects (font (size 1.27 1.27)) hide)
     )
+    (property "NOTES" "DO NOT POPULATE" (id 14) (at 101.6 100.33 0)
+      (effects (font (size 1.27 1.27)) hide)
+    )
     (pin "TP")
   )
@@
       (effects (font (size 1.27 1.27)) (justify bottom) hide)
     )
-    (property "PURCHASE-URL" "https://pricing.snapeda.com/search/part/5005/?ref=eda" (id 10) (at 184.15 100.33 0)
+    (property "PURCHASE-URL" "" (id 10) (at 184.15 100.33 0)
       (effects (font (size 1.27 1.27)) (justify bottom) hide)
     )
@@
       (effects (font (size 1.27 1.27)) hide)
     )
+    (property "NOTES" "DO NOT POPULATE" (id 14) (at 184.15 100.33 0)
+      (effects (font (size 1.27 1.27)) hide)
+    )
     (pin "TP")
   )
@@
       (effects (font (size 1.27 1.27)) (justify bottom) hide)
     )
-    (property "PURCHASE-URL" "https://pricing.snapeda.com/search/part/5005/?ref=eda" (id 10) (at 107.95 100.33 0)
+    (property "PURCHASE-URL" "" (id 10) (at 107.95 100.33 0)
       (effects (font (size 1.27 1.27)) (justify bottom) hide)
     )
@@
       (effects (font (size 1.27 1.27)) hide)
     )
+    (property "NOTES" "DO NOT POPULATE" (id 14) (at 107.95 100.33 0)
+      (effects (font (size 1.27 1.27)) hide)
+    )
     (pin "TP")
   )
@@
       (effects (font (size 1.27 1.27)) (justify bottom) hide)
     )
-    (property "PURCHASE-URL" "https://pricing.snapeda.com/search/part/5005/?ref=eda" (id 10) (at 120.65 100.33 0)
+    (property "PURCHASE-URL" "" (id 10) (at 120.65 100.33 0)
       (effects (font (size 1.27 1.27)) (justify bottom) hide)
     )
@@
       (effects (font (size 1.27 1.27)) hide)
     )
+    (property "NOTES" "DO NOT POPULATE" (id 14) (at 120.65 100.33 0)
+      (effects (font (size 1.27 1.27)) hide)
+    )
     (pin "TP")
   )
@@
       (effects (font (size 1.27 1.27)) (justify bottom) hide)
     )
-    (property "PURCHASE-URL" "https://pricing.snapeda.com/search/part/5005/?ref=eda" (id 10) (at 127 100.33 0)
+    (property "PURCHASE-URL" "" (id 10) (at 127 100.33 0)
       (effects (font (size 1.27 1.27)) (justify bottom) hide)
     )
@@
       (effects (font (size 1.27 1.27)) hide)
     )
+    (property "NOTES" "DO NOT POPULATE" (id 14) (at 127 100.33 0)
+      (effects (font (size 1.27 1.27)) hide)
+    )
     (pin "TP")
   )
@@
       (effects (font (size 1.27 1.27)) (justify bottom) hide)
     )
-    (property "PURCHASE-URL" "https://pricing.snapeda.com/search/part/5005/?ref=eda" (id 10) (at 165.1 100.33 0)
+    (property "PURCHASE-URL" "" (id 10) (at 165.1 100.33 0)
       (effects (font (size 1.27 1.27)) (justify bottom) hide)
     )
@@
       (effects (font (size 1.27 1.27)) hide)
     )
+    (property "NOTES" "DO NOT POPULATE" (id 14) (at 165.1 100.33 0)
+      (effects (font (size 1.27 1.27)) hide)
+    )
     (pin "TP")
   )
@@
       (effects (font (size 1.27 1.27)) (justify bottom) hide)
     )
-    (property "PURCHASE-URL" "https://pricing.snapeda.com/search/part/5005/?ref=eda" (id 10) (at 177.8 100.33 0)
+    (property "PURCHASE-URL" "" (id 10) (at 177.8 100.33 0)
       (effects (font (size 1.27 1.27)) (justify bottom) hide)
     )
@@
       (effects (font (size 1.27 1.27)) hide)
     )
+    (property "NOTES" "DO NOT POPULATE" (id 14) (at 177.8 100.33 0)
+      (effects (font (size 1.27 1.27)) hide)
+    )
     (pin "TP")
   )
@@
       (effects (font (size 1.27 1.27)) (justify bottom) hide)
     )
-    (property "PURCHASE-URL" "https://pricing.snapeda.com/search/part/5005/?ref=eda" (id 10) (at 114.3 100.33 0)
+    (property "PURCHASE-URL" "" (id 10) (at 114.3 100.33 0)
       (effects (font (size 1.27 1.27)) (justify bottom) hide)
     )
@@
       (effects (font (size 1.27 1.27)) hide)
     )
+    (property "NOTES" "DO NOT POPULATE" (id 14) (at 114.3 100.33 0)
+      (effects (font (size 1.27 1.27)) hide)
+    )
     (pin "TP")
   )
@@
       (effects (font (size 1.27 1.27)) (justify bottom) hide)
     )
-    (property "PURCHASE-URL" "https://pricing.snapeda.com/search/part/5005/?ref=eda" (id 10) (at 190.5 100.33 0)
+    (property "PURCHASE-URL" "" (id 10) (at 190.5 100.33 0)
       (effects (font (size 1.27 1.27)) (justify bottom) hide)
     )
@@
       (effects (font (size 1.27 1.27)) hide)
     )
+    (property "NOTES" "DO NOT POPULATE" (id 14) (at 190.5 100.33 0)
+      (effects (font (size 1.27 1.27)) hide)
+    )
